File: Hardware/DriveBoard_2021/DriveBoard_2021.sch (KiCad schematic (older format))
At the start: 87 parts, among them SW1 SW_Push, SW2 SW_Push, SW3 SW_Push, SW4 SW_Push, SW5 SW_Push, SW6 SW_Push, SW7 SW_Push, U1 TM4C129E_Launchpad, U2 LM2576S-3.3, U3 LM2576HVS-5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

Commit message: Added Footprint for all Components, started board
Switched ferrite beads to fuses
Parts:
- removed FB1, FB2: Ferrite_Bead_Small, symbol Device:Ferrite_Bead_Small
- added F1, F2: Fuse, MRDT_Passives:ATC_Fuse_Block, symbol Device:Fuse_Small
- ABS_ENC1, ABS_ENC2, ABS_ENC3, ABS_ENC4, BL_WHL1, BL_WHL2, FL_WHL1, FR_WHL1, SERIAL1, SERIAL2: footprint (none) -> MRDT_Connectors:MOLEX_SL_03_Horizontal
- C1, C3, C4: footprint (none) -> Capacitor_SMD:C_0603_1608Metric_Pad1.05x0.95mm_HandSolder
- C2: renamed from C3; footprint (none) -> Capacitor_SMD:C_0603_1608Metric_Pad1.05x0.95mm_HandSolder
- C5: renamed from C2; footprint (none) -> Capacitor_SMD:C_0603_1608Metric_Pad1.05x0.95mm_HandSolder
- C6: renamed from C4; footprint (none) -> Capacitor_SMD:C_0603_1608Metric_Pad1.05x0.95mm_HandSolder
- CAN1, CAN2: footprint (none) -> MRDT_Connectors:MOLEX_SL_02_Horizontal
- Conn1, Conn2, Conn3: footprint (none) -> MRDT_Connectors:Anderson_2_Horizontal_Side_by_Side
- L1, L2: footprint (none) -> Inductor_SMD:L_0603_1608Metric_Pad1.05x0.95mm_HandSolder
- LED1, LED4: footprint (none) -> LED_SMD:LED_0603_1608Metric_Pad1.05x0.95mm_HandSolder
- LED10: renamed from LED6; footprint (none) -> LED_SMD:LED_0603_1608Metric_Pad1.05x0.95mm_HandSolder
- LED11: renamed from LED7; footprint (none) -> LED_SMD:LED_0603_1608Metric_Pad1.05x0.95mm_HandSolder
- LED12: renamed from LED8; footprint (none) -> LED_SMD:LED_0603_1608Metric_Pad1.05x0.95mm_HandSolder
- LED13: renamed from LED9; footprint (none) -> LED_SMD:LED_0603_1608Metric_Pad1.05x0.95mm_HandSolder
- LED14, LED22: renamed from LED16; footprint (none) -> LED_SMD:LED_0603_1608Metric_Pad1.05x0.95mm_HandSolder
- LED15, LED23: renamed from LED17; footprint (none) -> LED_SMD:LED_0603_1608Metric_Pad1.05x0.95mm_HandSolder
- LED16: renamed from LED2; footprint (none) -> LED_SMD:LED_0603_1608Metric_Pad1.05x0.95mm_HandSolder
- LED17: renamed from LED10; footprint (none) -> LED_SMD:LED_0603_1608Metric_Pad1.05x0.95mm_HandSolder
- LED18: renamed from LED11; footprint (none) -> LED_SMD:LED_0603_1608Metric_Pad1.05x0.95mm_HandSolder
- LED19, LED6: renamed from LED13; footprint (none) -> LED_SMD:LED_0603_1608Metric_Pad1.05x0.95mm_HandSolder
- LED2: renamed from LED3; footprint (none) -> LED_SMD:LED_0603_1608Metric_Pad1.05x0.95mm_HandSolder
- LED20, LED7: renamed from LED14; footprint (none) -> LED_SMD:LED_0603_1608Metric_Pad1.05x0.95mm_HandSolder
- LED21, LED8: renamed from LED15; footprint (none) -> LED_SMD:LED_0603_1608Metric_Pad1.05x0.95mm_HandSolder
- LED24: renamed from LED18; footprint (none) -> LED_SMD:LED_0603_1608Metric_Pad1.05x0.95mm_HandSolder
- LED3, LED5: renamed from LED12; footprint (none) -> LED_SMD:LED_0603_1608Metric_Pad1.05x0.95mm_HandSolder
- LED9: renamed from LED5; footprint (none) -> LED_SMD:LED_0603_1608Metric_Pad1.05x0.95mm_HandSolder
- R1: renamed from R11; footprint (none) -> Resistor_SMD:R_0603_1608Metric_Pad1.05x0.95mm_HandSolder
- R10: renamed from R3; footprint (none) -> Resistor_SMD:R_0603_1608Metric_Pad1.05x0.95mm_HandSolder
- R11: renamed from R4; footprint (none) -> Resistor_SMD:R_0603_1608Metric_Pad1.05x0.95mm_HandSolder
- R12: renamed from R5; footprint (none) -> Resistor_SMD:R_0603_1608Metric_Pad1.05x0.95mm_HandSolder
- R13: renamed from R16; footprint (none) -> Resistor_SMD:R_0603_1608Metric_Pad1.05x0.95mm_HandSolder
- R14: renamed from R17; footprint (none) -> Resistor_SMD:R_0603_1608Metric_Pad1.05x0.95mm_HandSolder
- R15: renamed from R26; footprint (none) -> Resistor_SMD:R_0603_1608Metric_Pad1.05x0.95mm_HandSolder
- R16: renamed from R6; footprint (none) -> Resistor_SMD:R_0603_1608Metric_Pad1.05x0.95mm_HandSolder
- R17: renamed from R7; footprint (none) -> Resistor_SMD:R_0603_1608Metric_Pad1.05x0.95mm_HandSolder
- R18: renamed from R8; footprint (none) -> Resistor_SMD:R_0603_1608Metric_Pad1.05x0.95mm_HandSolder
- R19: renamed from R20; footprint (none) -> Resistor_SMD:R_0603_1608Metric_Pad1.05x0.95mm_HandSolder
- R2: renamed from R9; footprint (none) -> Resistor_SMD:R_0603_1608Metric_Pad1.05x0.95mm_HandSolder
- R20: renamed from R21; footprint (none) -> Resistor_SMD:R_0603_1608Metric_Pad1.05x0.95mm_HandSolder
- R21: renamed from R22; footprint (none) -> Resistor_SMD:R_0603_1608Metric_Pad1.05x0.95mm_HandSolder
- R22: renamed from R23; footprint (none) -> Resistor_SMD:R_0603_1608Metric_Pad1.05x0.95mm_HandSolder
- R23: renamed from R24; footprint (none) -> Resistor_SMD:R_0603_1608Metric_Pad1.05x0.95mm_HandSolder
- R24: renamed from R25; footprint (none) -> Resistor_SMD:R_0603_1608Metric_Pad1.05x0.95mm_HandSolder
- R25: renamed from R18; footprint (none) -> Resistor_SMD:R_0603_1608Metric_Pad1.05x0.95mm_HandSolder
- R3: renamed from R19; footprint (none) -> Resistor_SMD:R_0603_1608Metric_Pad1.05x0.95mm_HandSolder
- R4: renamed from R12; footprint (none) -> Resistor_SMD:R_0603_1608Metric_Pad1.05x0.95mm_HandSolder
- R5: renamed from R13; footprint (none) -> Resistor_SMD:R_0603_1608Metric_Pad1.05x0.95mm_HandSolder
- R6: renamed from R14; footprint (none) -> Resistor_SMD:R_0603_1608Metric_Pad1.05x0.95mm_HandSolder
- R7: renamed from R15; footprint (none) -> Resistor_SMD:R_0603_1608Metric_Pad1.05x0.95mm_HandSolder
- R8: renamed from R1; footprint (none) -> Resistor_SMD:R_0603_1608Metric_Pad1.05x0.95mm_HandSolder
- R9: renamed from R2; footprint (none) -> Resistor_SMD:R_0603_1608Metric_Pad1.05x0.95mm_HandSolder
- SW1, SW2, SW3, SW4, SW5, SW6, SW7: footprint (none) -> Button_Switch_SMD:SW_SPST_TL3305A
- U3: renamed from U1; footprint (none) -> MRDT_Shields:TM4C129E_Launchpad_FULL_SMD_BOTTOM
- renumbered U2 to U1, U3 to U2

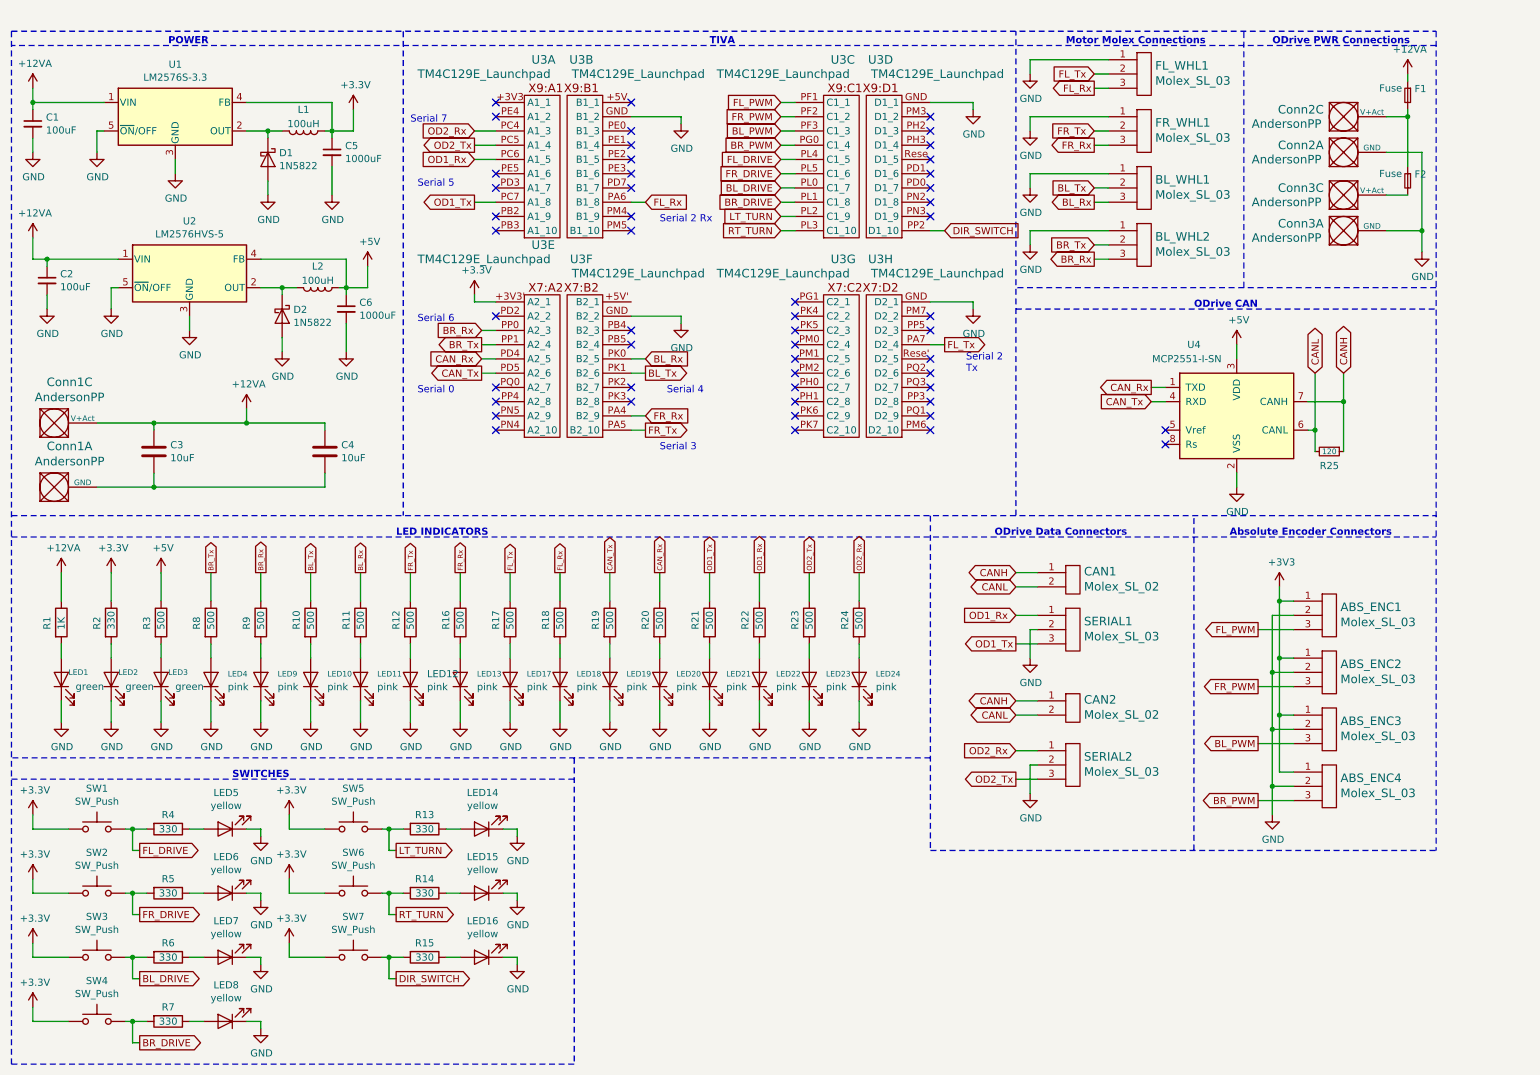
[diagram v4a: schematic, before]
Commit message: Added 12V logic line
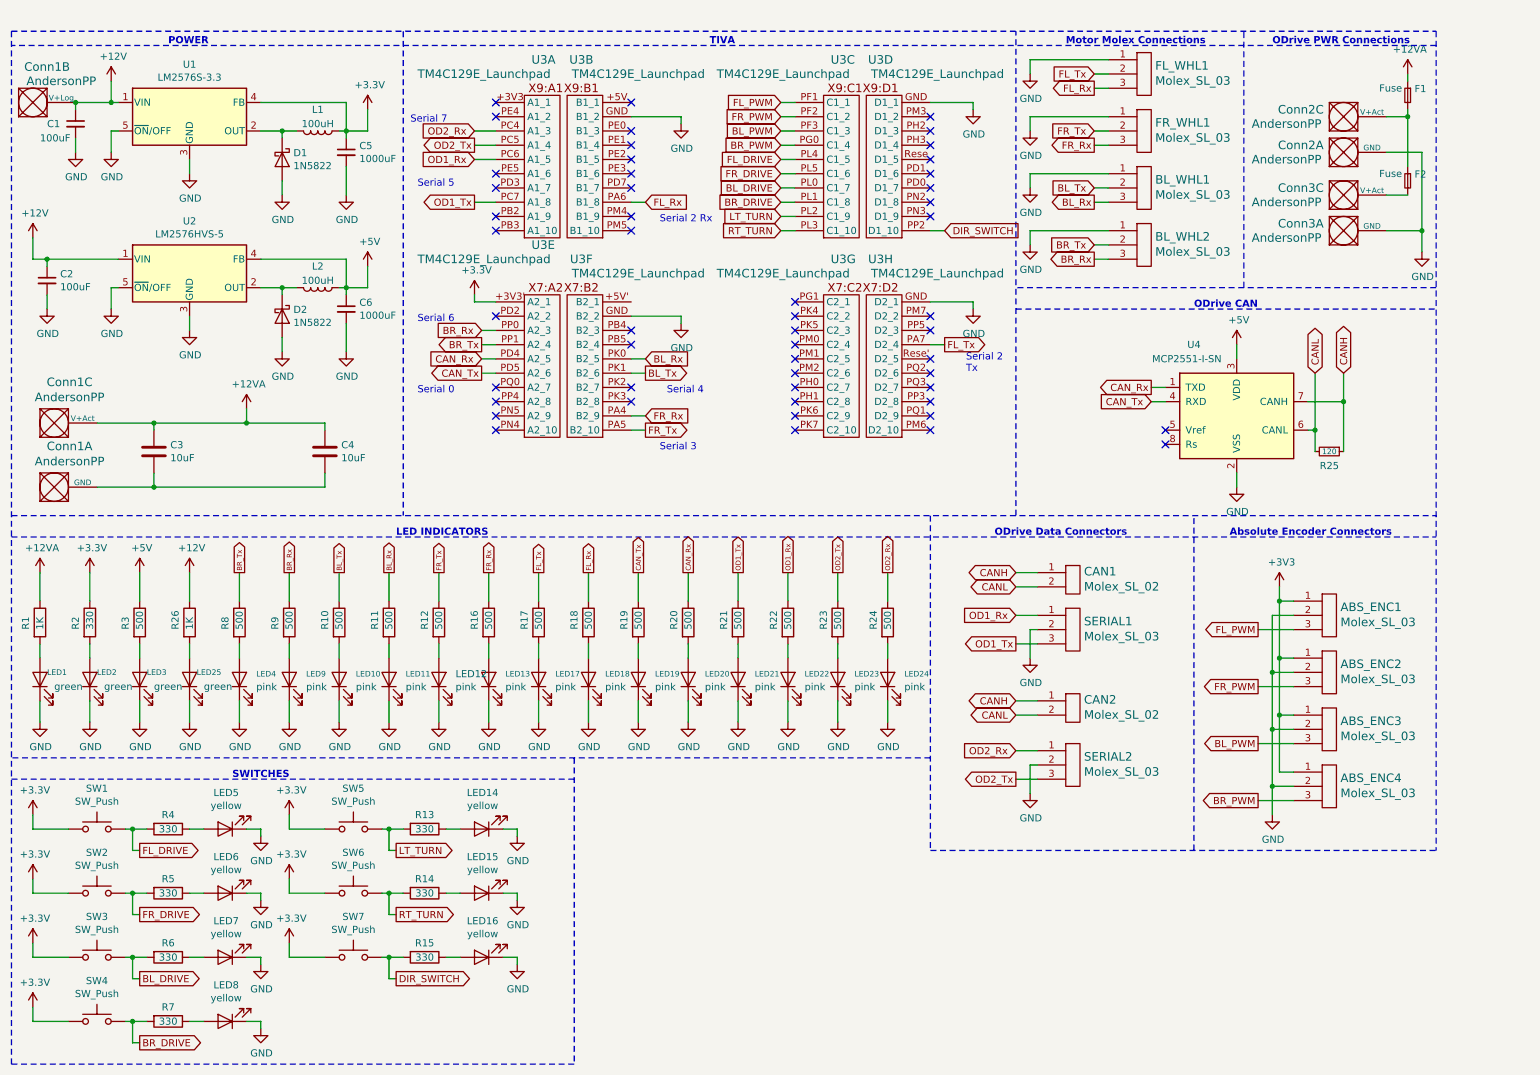
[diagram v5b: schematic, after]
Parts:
- added unit 2 of Conn1
- added LED25: green, LED_SMD:LED_0603_1608Metric_Pad1.05x0.95mm_HandSolder, symbol Device:LED
- added R26: 1K, Resistor_SMD:R_0603_1608Metric_Pad1.05x0.95mm_HandSolder, symbol Device:R
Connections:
- net +12VA: no longer C1.1, C2.1, U1.1 (VIN), U2.1 (VIN)
- net GND: now also LED25.1 (K)
- new net: LED25.2 (A), R26.2
- new net +12V: C1.1, C2.1, Conn1.2 (V+Log), R26.1, U1.1 (VIN), U2.1 (VIN)
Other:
- moved on the sheet: C1, C5, D1, L1, LED1, LED10, LED11, LED12, LED13, LED17, LED18, LED19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

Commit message: Odrive Pads Updated, Board Outline Finished, Andersons added to board
12VA pin on anderson symbol was re-assigned to work on pad 2 for 2 port anderson connector.
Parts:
- Conn1: footprint MRDT_Connectors:Anderson_2_Horizontal_Side_by_Side -> MRDT_Connectors:Anderson_3_Horizontal_Side_by_Side
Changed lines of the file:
@@
 F 0 "Conn1" H 908 4187 60  0000 C CNN
 F 1 "AndersonPP" H 908 4081 60  0000 C CNN
-F 2 "MRDT_Connectors:Anderson_2_Horizontal_Side_by_Side" H 550 3250 60  0001 C CNN
+F 2 "MRDT_Connectors:Anderson_3_Horizontal_Side_by_Side" H 550 3250 60  0001 C CNN
 F 3 "" H 550 3250 60  0001 C CNN
 	1    700  3800
@@
 F 3 "" H 9600 900 60  0001 C CNN
 	1    9750 1450
-	1    0    0    -1
-$EndComp
-$Comp
-L MRDT_Connectors:AndersonPP Conn2
-U 3 1 5F8BFD78
-P 9750 1200
-F 0 "Conn2" H 9550 1350 60  0000 C CNN
-F 1 "AndersonPP" H 9450 1250 60  0000 C CNN
-F 2 "MRDT_Connectors:Anderson_2_Horizontal_Side_by_Side" H 9600 650 60  0001 C CNN
-F 3 "" H 9600 650 60  0001 C CNN
-	3    9750 1200
 	1    0    0    -1
 $EndComp
@@
 F 0 "Conn1" H 908 3737 60  0000 C CNN
 F 1 "AndersonPP" H 908 3631 60  0000 C CNN
-F 2 "MRDT_Connectors:Anderson_2_Horizontal_Side_by_Side" H 550 2800 60  0001 C CNN
+F 2 "MRDT_Connectors:Anderson_3_Horizontal_Side_by_Side" H 550 2800 60  0001 C CNN
 F 3 "" H 550 2800 60  0001 C CNN
 	3    700  3350
@@
 F 0 "Conn1" H 750 1450 60  0000 C CNN
 F 1 "AndersonPP" H 850 1350 60  0000 C CNN
-F 2 "MRDT_Connectors:Anderson_2_Horizontal_Side_by_Side" H 400 550 60  0001 C CNN
+F 2 "MRDT_Connectors:Anderson_3_Horizontal_Side_by_Side" H 400 550 60  0001 C CNN
 F 3 "" H 400 550 60  0001 C CNN
 	2    550  1100
@@
 	1    0    0    -1
 $EndComp
+$Comp
+L MRDT_Connectors:AndersonPP Conn2
+U 3 1 5F8BFD78
+P 9750 1200
+F 0 "Conn2" H 9550 1350 60  0000 C CNN
+F 1 "AndersonPP" H 9450 1250 60  0000 C CNN
+F 2 "MRDT_Connectors:Anderson_2_Horizontal_Side_by_Side" H 9600 650 60  0001 C CNN
+F 3 "" H 9600 650 60  0001 C CNN
+	3    9750 1200
+	1    0    0    -1
+$EndComp

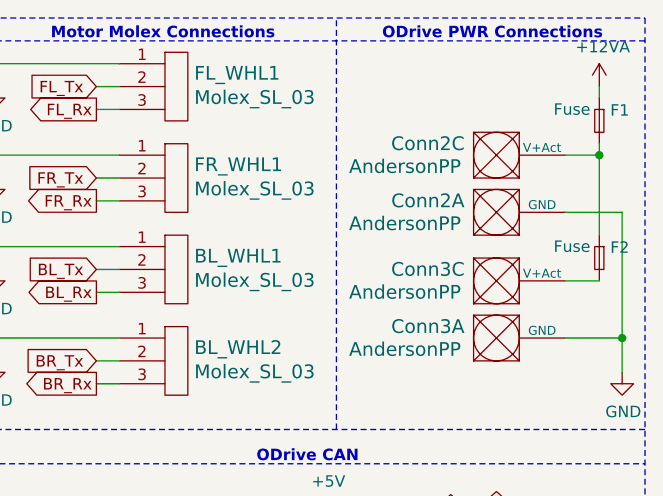
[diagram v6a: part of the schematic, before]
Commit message: Fixed pad issue for PWR in. Added bucks to board.
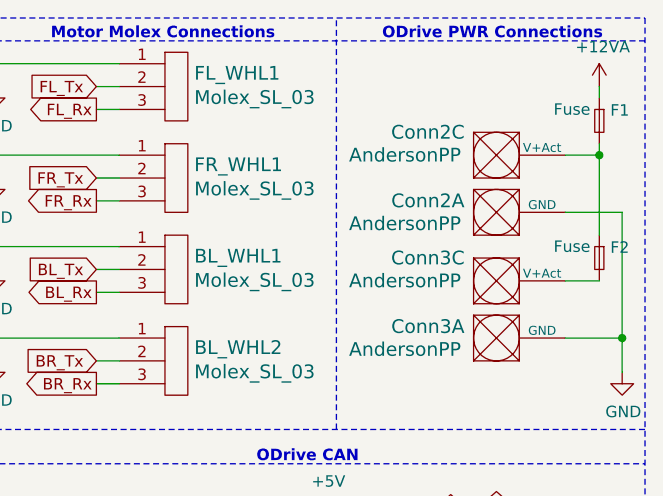
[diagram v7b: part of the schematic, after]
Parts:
- removed Conn2, Conn3: AndersonPP, MRDT_Connectors:Anderson_2_Horizontal_Side_by_Side, symbol MRDT_Connectors:AndersonPP
- added Conn2, Conn3: AndersonPP, MRDT_Connectors:Anderson_2_Horizontal_Side_by_Side, symbol MRDT_Connectors:AndersonPP_GND_VA
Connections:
- net GND: now also Conn2.1 (GND), Conn3.1 (GND)
- net at F1.2, F2.1: now also Conn2.2 (V+Act)
- net at F2.2: now also Conn3.2 (V+Act)
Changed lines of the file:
@@
 Text Notes 7900 600  0    50   ~ 10
 Motor Molex Connections
-$Comp
-L MRDT_Connectors:AndersonPP Conn2
-U 1 1 5F8B4265
-P 9750 1450
-F 0 "Conn2" H 9550 1600 60  0000 C CNN
-F 1 "AndersonPP" H 9450 1500 60  0000 C CNN
-F 2 "MRDT_Connectors:Anderson_2_Horizontal_Side_by_Side" H 9600 900 60  0001 C CNN
-F 3 "" H 9600 900 60  0001 C CNN
-	1    9750 1450
-	1    0    0    -1
-$EndComp
-$Comp
-L MRDT_Connectors:AndersonPP Conn3
-U 1 1 5F8DB853
-P 9750 2000
-F 0 "Conn3" H 9550 2150 60  0000 C CNN
-F 1 "AndersonPP" H 9450 2050 60  0000 C CNN
-F 2 "MRDT_Connectors:Anderson_2_Horizontal_Side_by_Side" H 9600 1450 60  0001 C CNN
-F 3 "" H 9600 1450 60  0001 C CNN
-	1    9750 2000
-	1    0    0    -1
-$EndComp
-$Comp
-L MRDT_Connectors:AndersonPP Conn3
-U 3 1 5F8DB859
-P 9750 1750
-F 0 "Conn3" H 9550 1900 60  0000 C CNN
-F 1 "AndersonPP" H 9450 1800 60  0000 C CNN
-F 2 "MRDT_Connectors:Anderson_2_Horizontal_Side_by_Side" H 9600 1200 60  0001 C CNN
-F 3 "" H 9600 1200 60  0001 C CNN
-	3    9750 1750
-	1    0    0    -1
-$EndComp
 Wire Wire Line
 	10300 1100 10150 1100
@@
 $EndComp
 $Comp
-L MRDT_Connectors:AndersonPP Conn2
-U 3 1 5F8BFD78
+L MRDT_Connectors:AndersonPP_GND_VA Conn2
+U 3 1 5FC54952
 P 9750 1200
-F 0 "Conn2" H 9550 1350 60  0000 C CNN
-F 1 "AndersonPP" H 9450 1250 60  0000 C CNN
+F 0 "Conn2" H 9550 1400 60  0000 C CNN
+F 1 "AndersonPP" H 9450 1300 60  0000 C CNN
 F 2 "MRDT_Connectors:Anderson_2_Horizontal_Side_by_Side" H 9600 650 60  0001 C CNN
 F 3 "" H 9600 650 60  0001 C CNN
@@
 	1    0    0    -1
 $EndComp
+$Comp
+L MRDT_Connectors:AndersonPP_GND_VA Conn2
+U 1 1 5FC56CA6
+P 9750 1450
+F 0 "Conn2" H 9550 1600 60  0000 C CNN
+F 1 "AndersonPP" H 9450 1500 60  0000 C CNN
+F 2 "MRDT_Connectors:Anderson_2_Horizontal_Side_by_Side" H 9600 900 60  0001 C CNN
+F 3 "" H 9600 900 60  0001 C CNN
+	1    9750 1450
+	1    0    0    -1
+$EndComp
+$Comp
+L MRDT_Connectors:AndersonPP_GND_VA Conn3
+U 3 1 5FC757F7
+P 9750 1750
+F 0 "Conn3" H 9550 1950 60  0000 C CNN
+F 1 "AndersonPP" H 9450 1850 60  0000 C CNN
+F 2 "MRDT_Connectors:Anderson_2_Horizontal_Side_by_Side" H 9600 1200 60  0001 C CNN
+F 3 "" H 9600 1200 60  0001 C CNN
+	3    9750 1750
+	1    0    0    -1
+$EndComp
+$Comp
+L MRDT_Connectors:AndersonPP_GND_VA Conn3
+U 1 1 5FC757FD
+P 9750 2000
+F 0 "Conn3" H 9550 2150 60  0000 C CNN
+F 1 "AndersonPP" H 9450 2050 60  0000 C CNN
+F 2 "MRDT_Connectors:Anderson_2_Horizontal_Side_by_Side" H 9600 1450 60  0001 C CNN
+F 3 "" H 9600 1450 60  0001 C CNN
+	1    9750 2000
+	1    0    0    -1
+$EndComp
